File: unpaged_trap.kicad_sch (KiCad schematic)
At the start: 12 parts

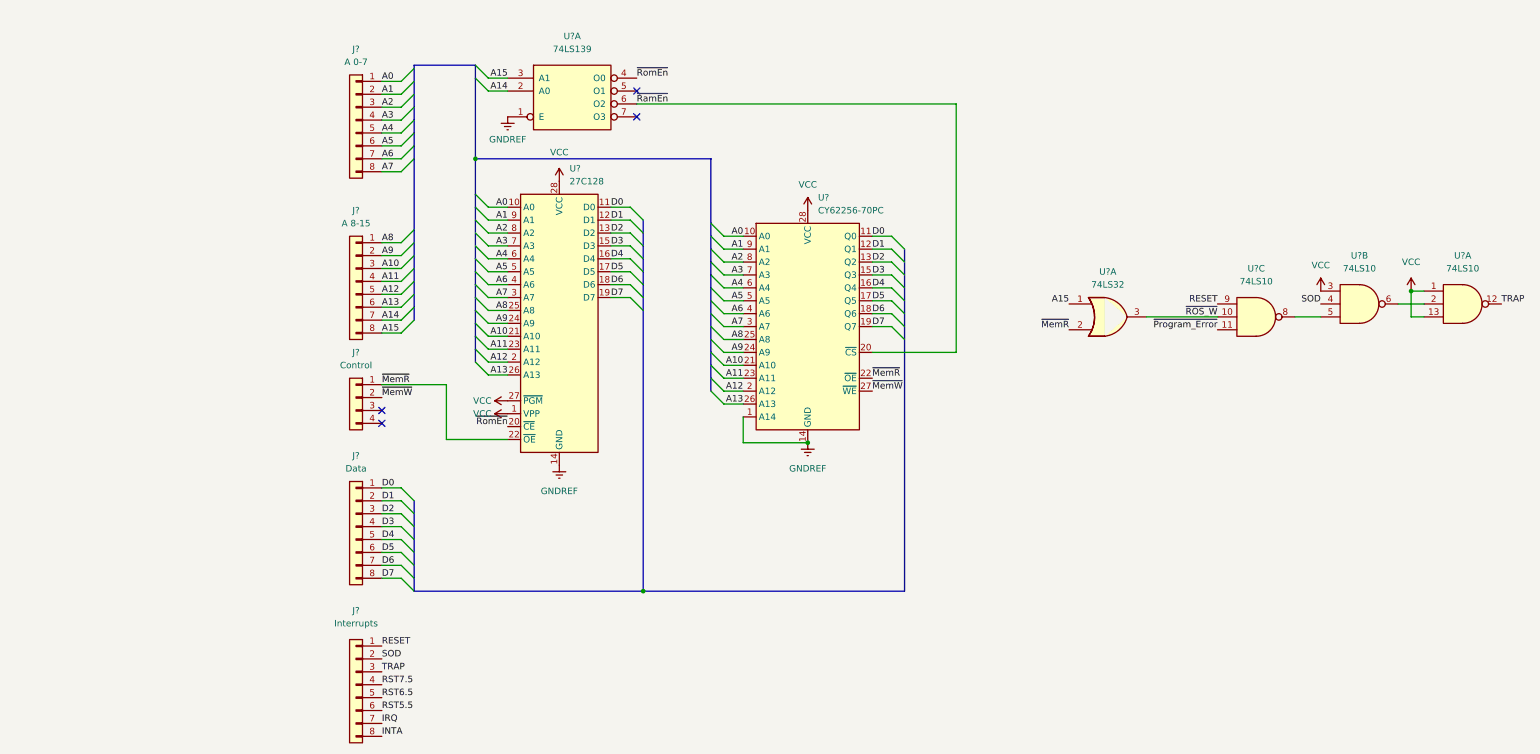
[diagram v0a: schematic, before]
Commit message: Updated to version 8
Changed to version 8; added 96-pin connectors; described ports at PPI_Settings
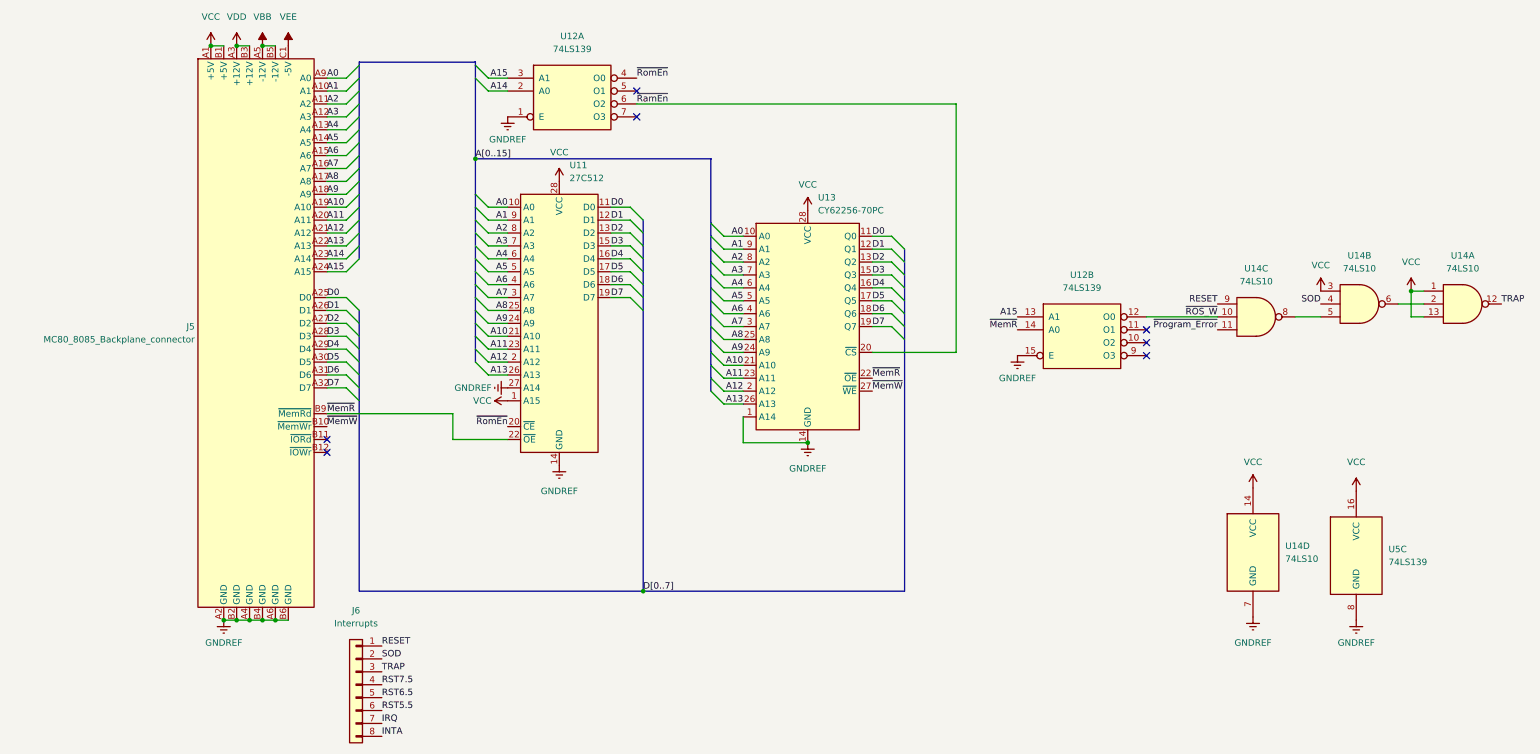
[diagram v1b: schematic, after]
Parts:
- removed J?: A 0-7, symbol Connector_Generic:Conn_01x08
- removed J?: A 8-15, symbol Connector_Generic:Conn_01x08
- removed J?: Control, symbol Connector_Generic:Conn_01x04
- removed J?: Data, symbol Connector_Generic:Conn_01x08
- removed U?: 27C128, Package_DIP:DIP-28_W15.24mm, symbol Memory_EPROM:27C128
- removed U?: 74LS32, symbol 74xx:74LS32
- added J5: MC80_8085_Backplane_connector, symbol connector-miscellaneous:MC80_8085_Backplane_connector
- added U11: 27C512, Package_DIP:DIP-28_W15.24mm, symbol Memory_EPROM:27C512
- added unit 2 of U12
- added unit 4 of U14
- added U5: 74LS139, symbol 74xx:74LS139
- gave numbers to parts that had none: 4
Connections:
- net A0: now also J5.A9 (A0), U11.10 (A0)
- net A1: now also J5.A10 (A1), U11.9 (A1)
- net A10: now also J5.A19 (A10), U11.21 (A10)
- net A11: now also J5.A20 (A11), U11.23 (A11)
- net A12: now also J5.A21 (A12), U11.2 (A12)
- net A13: now also J5.A22 (A13), U11.26 (A13)
- net A14: now also J5.A23 (A14)
- net A15: now also J5.A24 (A15), U12.13 (A1)
- net A2: now also J5.A11 (A2), U11.8 (A2)
- net A3: now also J5.A12 (A3), U11.7 (A3)
- net A4: now also J5.A13 (A4), U11.6 (A4)
- net A5: now also J5.A14 (A5), U11.5 (A5)
- net A6: now also J5.A15 (A6), U11.4 (A6)
- net A7: now also J5.A16 (A7), U11.3 (A7)
- net A8: now also J5.A17 (A8), U11.25 (A8)
- net A9: now also J5.A18 (A9), U11.24 (A9)
- net D0: now also J5.A25 (D0), U11.11 (D0)
- net D1: now also J5.A26 (D1), U11.12 (D1)
- net D2: now also J5.A27 (D2), U11.13 (D2)
- net D3: now also J5.A28 (D3), U11.15 (D3)
- net D4: now also J5.A29 (D4), U11.16 (D4)
- net D5: now also J5.A30 (D5), U11.17 (D5)
- net D6: now also J5.A31 (D6), U11.18 (D6)
- net D7: now also J5.A32 (D7), U11.19 (D7)
- net GNDREF: now also J5.A2 (GND), J5.A4 (GND), J5.A6 (GND), J5.B2 (GND), J5.B4 (GND), J5.B6 (GND), U11.14 (GND), U11.27 (A14), U12.15 (E), U14.7 (GND), U5.8 (GND)
- net VCC: now also J5.A1 (+5V), J5.B1 (+5V), U11.1 (A15), U11.28 (VCC), U14.14 (VCC), U5.16 (VCC)
- net ~{MemR}: now also J5.B9 (~{MemRd}), U11.22 (~{OE}), U12.14 (A0)
- net ~{MemW}: now also J5.B10 (~{MemWr})
- net ~{ROS_W}: now also U12.12 (O0)
- net ~{RomEn}: now also U11.20 (~{CE})
- new net VBB: J5.A5 (-12V), J5.B5 (-12V)
- new net VDD: J5.A3 (+12V), J5.B3 (+12V)
- new net VEE: J5.C1 (-5V)
- no-connect marks 4 -> 7
